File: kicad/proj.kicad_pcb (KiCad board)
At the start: 2 copper layers, 254 x 127 mm, 65 parts, among them J1 USB-C, J2 OLED, J3 USB-A, SW1 SW_DIP_x01, SW10 SW_DIP_x01, SW11 SW_DIP_x01, SW12 SW_DIP_x01, SW13 SW_DIP_x01, SW14 SW_DIP_x01, SW15 SW_DIP_x01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

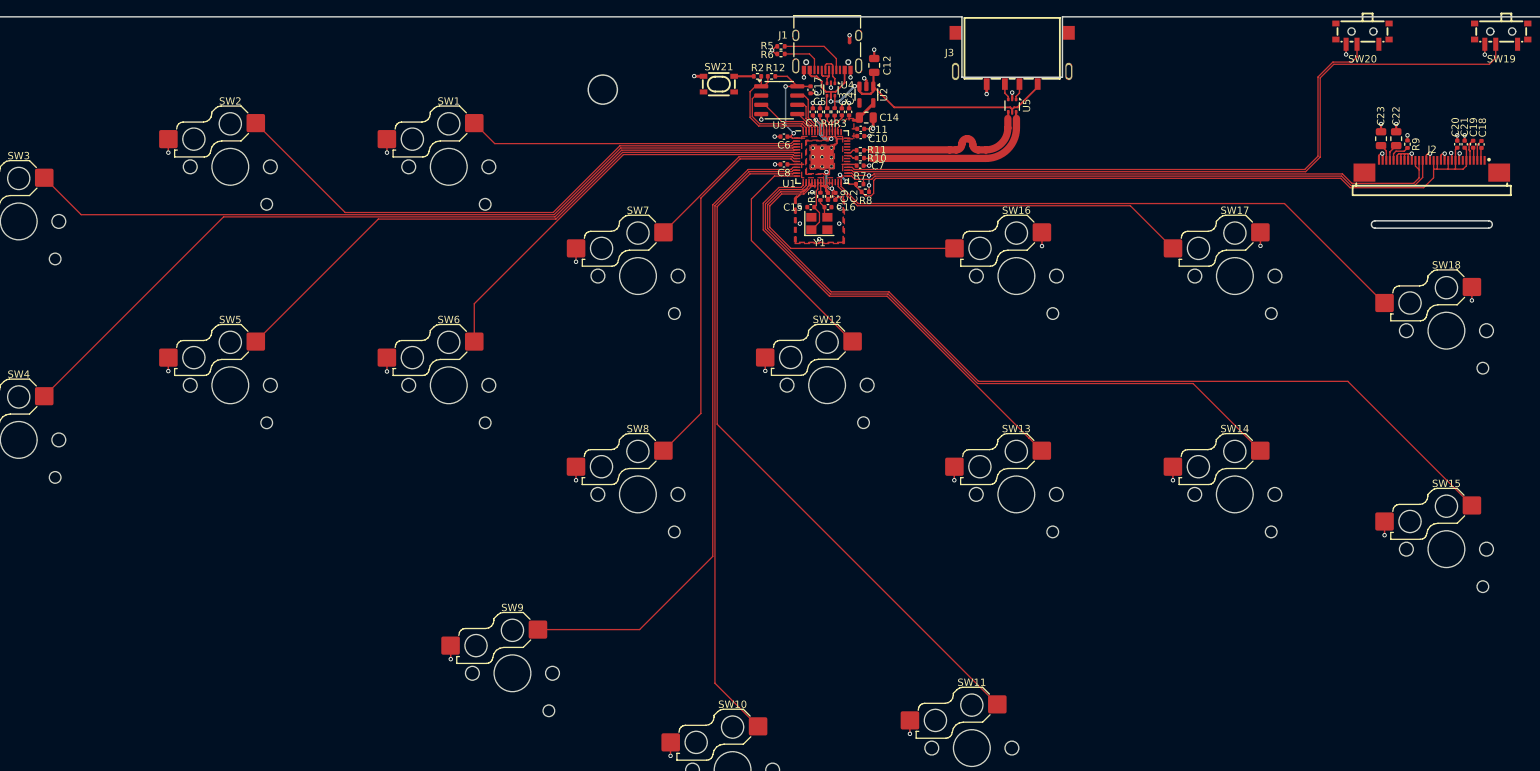
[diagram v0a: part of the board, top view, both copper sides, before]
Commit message: fillet trace corners
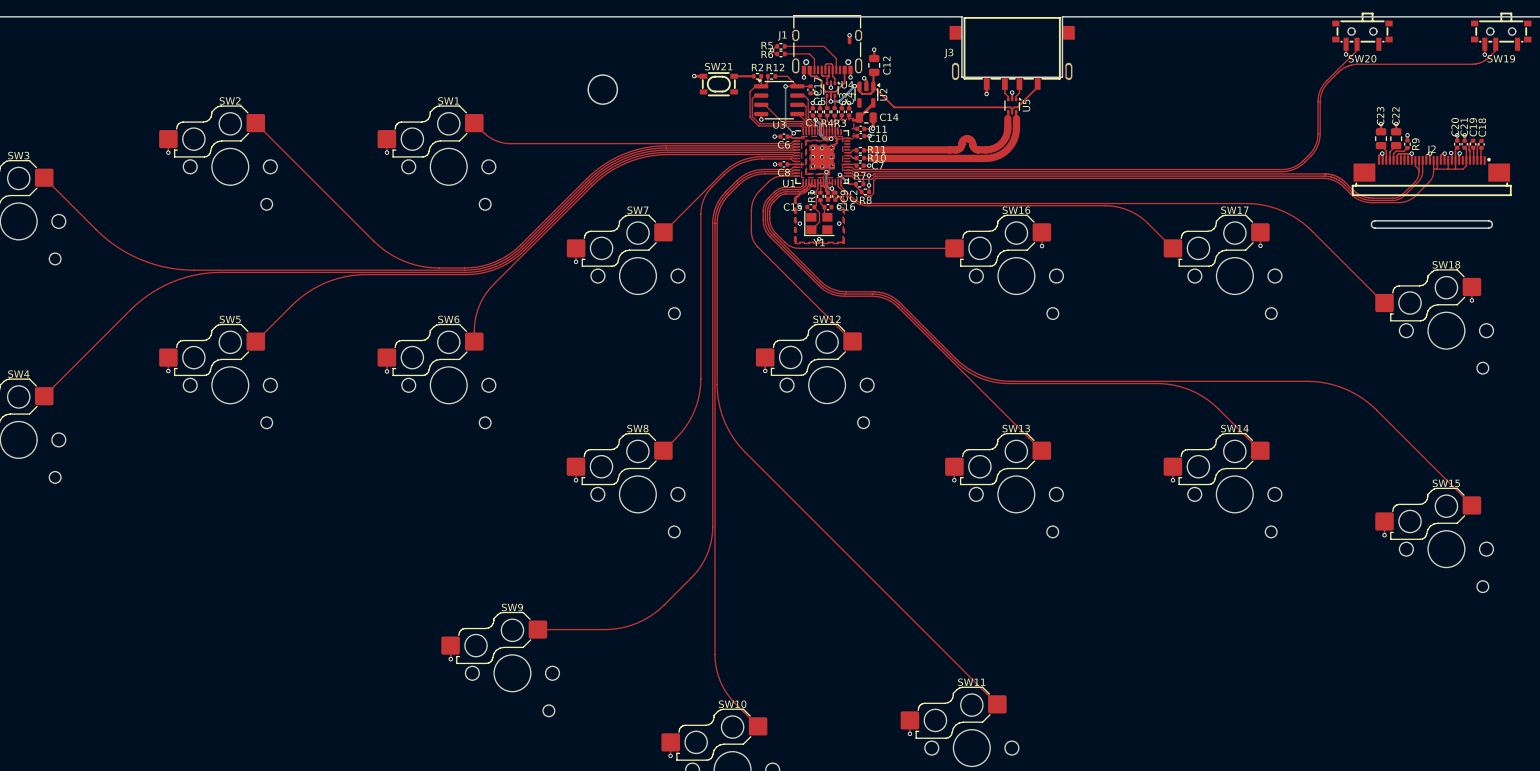
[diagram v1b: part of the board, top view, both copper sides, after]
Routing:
- net /GPIO1: track 83.3 -> 87.8 mm
- net /GPIO2: track 109.3 -> 113.5 mm
- net /GPIO20: track 103.9 -> 100.5 mm
- net /GPIO21: track 84.7 -> 81.7 mm
- net /GPIO3: track 117.4 -> 115.3 mm
- net /GPIO14: track 123.0 -> 120.9 mm
- net /GPIO4: track 85.1 -> 83.2 mm
- net /GPIO13: track 91.1 -> 89.2 mm
- net /GPIO8: track 90.2 -> 88.6 mm
- net /GPIO7: track 52.4 -> 51.2 mm
- net /GPIO19: track 85.7 -> 86.9 mm
- net /GPIO10: track 97.2 -> 96.0 mm
- net /GPIO5: track 58.1 -> 56.9 mm
- net /GPIO18: track 83.4 -> 84.5 mm
- net +3V3: track 136.4 -> 137.5 mm
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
